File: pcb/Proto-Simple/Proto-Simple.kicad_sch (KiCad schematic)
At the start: 21 parts, among them J1 Conn_01x04, J10 Conn_01x01, J11 Conn_01x01, J12 Conn_01x01, J13 Conn_01x01, J2 Conn_01x01, J3 Conn_01x01, J4 Conn_01x01, J41 Conn_01x01, J42 Conn_01x01, J43 Conn_01x01, J44 Conn_01x01, J45 Conn_01x01, J46 Conn_01x01, J47 Conn_01x01, J5 Conn_01x01, J6 Conn_01x01, J7 Conn_01x01, J8 Conn_01x01, J9 Conn_01x01

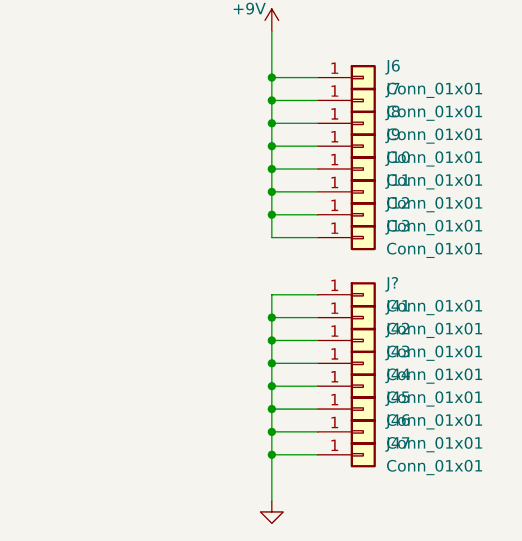
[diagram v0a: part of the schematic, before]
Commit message: [ProtoSimple] update Schematic
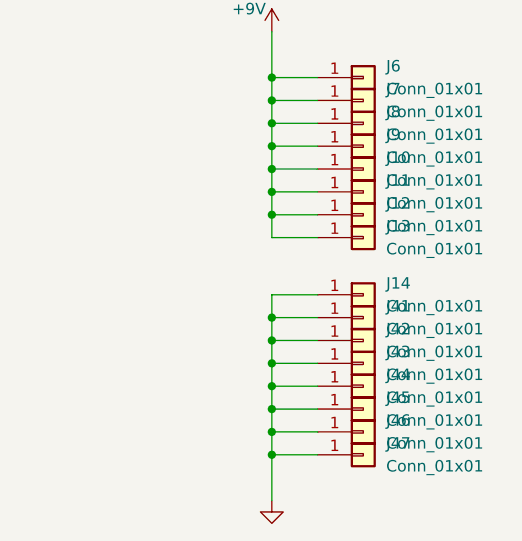
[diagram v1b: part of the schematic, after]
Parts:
- gave numbers to parts that had none: 1
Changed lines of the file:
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@@
   (symbol (lib_id "Connector_Generic:Conn_01x01") (at 163.83 119.38 0) (unit 1)
     (in_bom yes) (on_board yes) (fields_autoplaced)
-    (property "Reference" "J?" (id 0) (at 166.37 118.1099 0)
+    (property "Reference" "J14" (id 0) (at 166.37 118.1099 0)
       (effects (font (size 1.27 1.27)) (justify left))
     )
@@
       (reference "J13") (unit 1) (value "Conn_01x01") (footprint "MeineBib:Protopin")
     )
+    (path "/f7a1fee7-d81c-4e02-8116-b09f7e2d95c2"
+      (reference "J14") (unit 1) (value "Conn_01x01") (footprint "MeineBib:Protopin")
+    )
     (path "/2f3efa35-c3e1-45a2-83bc-04184a4ef9cc"
       (reference "J41") (unit 1) (value "Conn_01x01") (footprint "MeineBib:Protopin")
@@
       (reference "J47") (unit 1) (value "Conn_01x01") (footprint "MeineBib:Protopin")
     )
-    (path "/f7a1fee7-d81c-4e02-8116-b09f7e2d95c2"
-      (reference "J?") (unit 1) (value "Conn_01x01") (footprint "MeineBib:Protopin")
-    )
   )

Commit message: [All] Add LCSC part number for JST connector
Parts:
- J1: value Conn_01x04 -> (none); footprint Connector_JST:JST_XH_B4B-XH-A_1x04_P2.50mm_Vertical -> (none); LCSC^ (none) -> C144395; now in the parts list
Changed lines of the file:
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@@
   )
   (symbol (lib_id "Connector_Generic:Conn_01x04") (at 48.26 29.21 0) (mirror x) (unit 1)
-    (in_bom no) (on_board yes)
+    (in_bom yes) (on_board yes)
     (property "Reference" "J1" (id 0) (at 51.435 29.2101 0)
       (effects (font (size 1.27 1.27)) (justify left))
     )
-    (property "Value" "Conn_01x04" (id 1) (at 44.45 21.59 0)
+    (property "Value" "" (id 1) (at 44.45 21.59 0)
       (effects (font (size 1.27 1.27)) (justify left))
     )
-    (property "Footprint" "Connector_JST:JST_XH_B4B-XH-A_1x04_P2.50mm_Vertical" (id 2) (at 48.26 29.21 0)
+    (property "Footprint" "" (id 2) (at 48.26 29.21 0)
       (effects (font (size 1.27 1.27)) hide)
     )
@@
       (effects (font (size 1.27 1.27)) hide)
     )
+    (property "LCSC^" "C144395" (id 4) (at 48.26 29.21 0)
+      (effects (font (size 1.27 1.27)) hide)
+    )

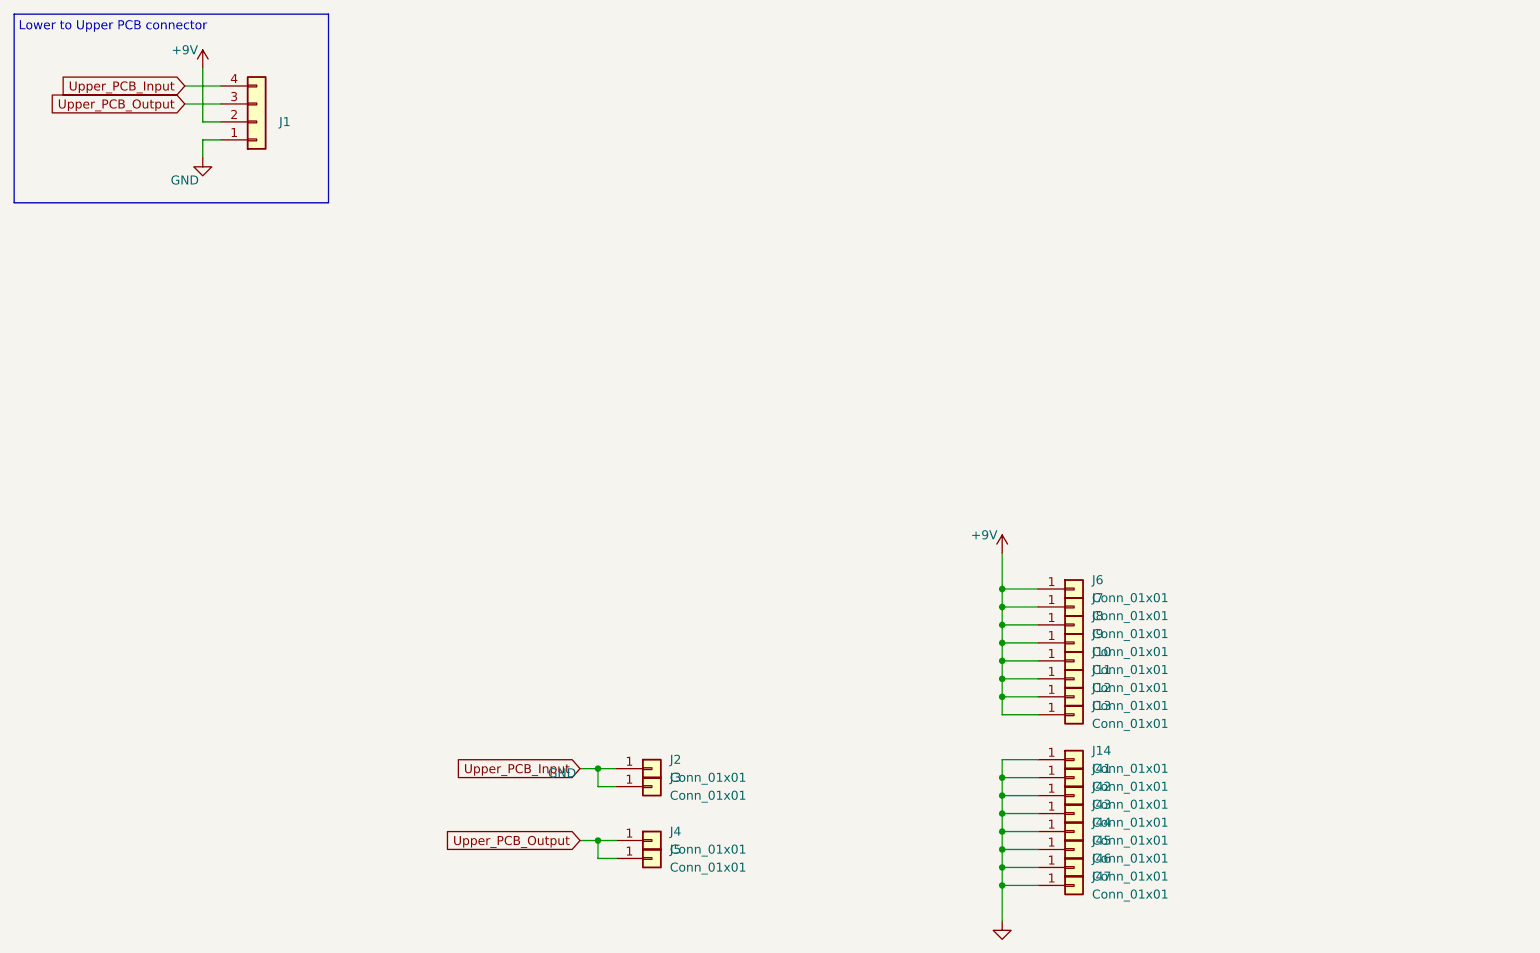
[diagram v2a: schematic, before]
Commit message: [ProtoSimple] Recreate PCB according to new base template
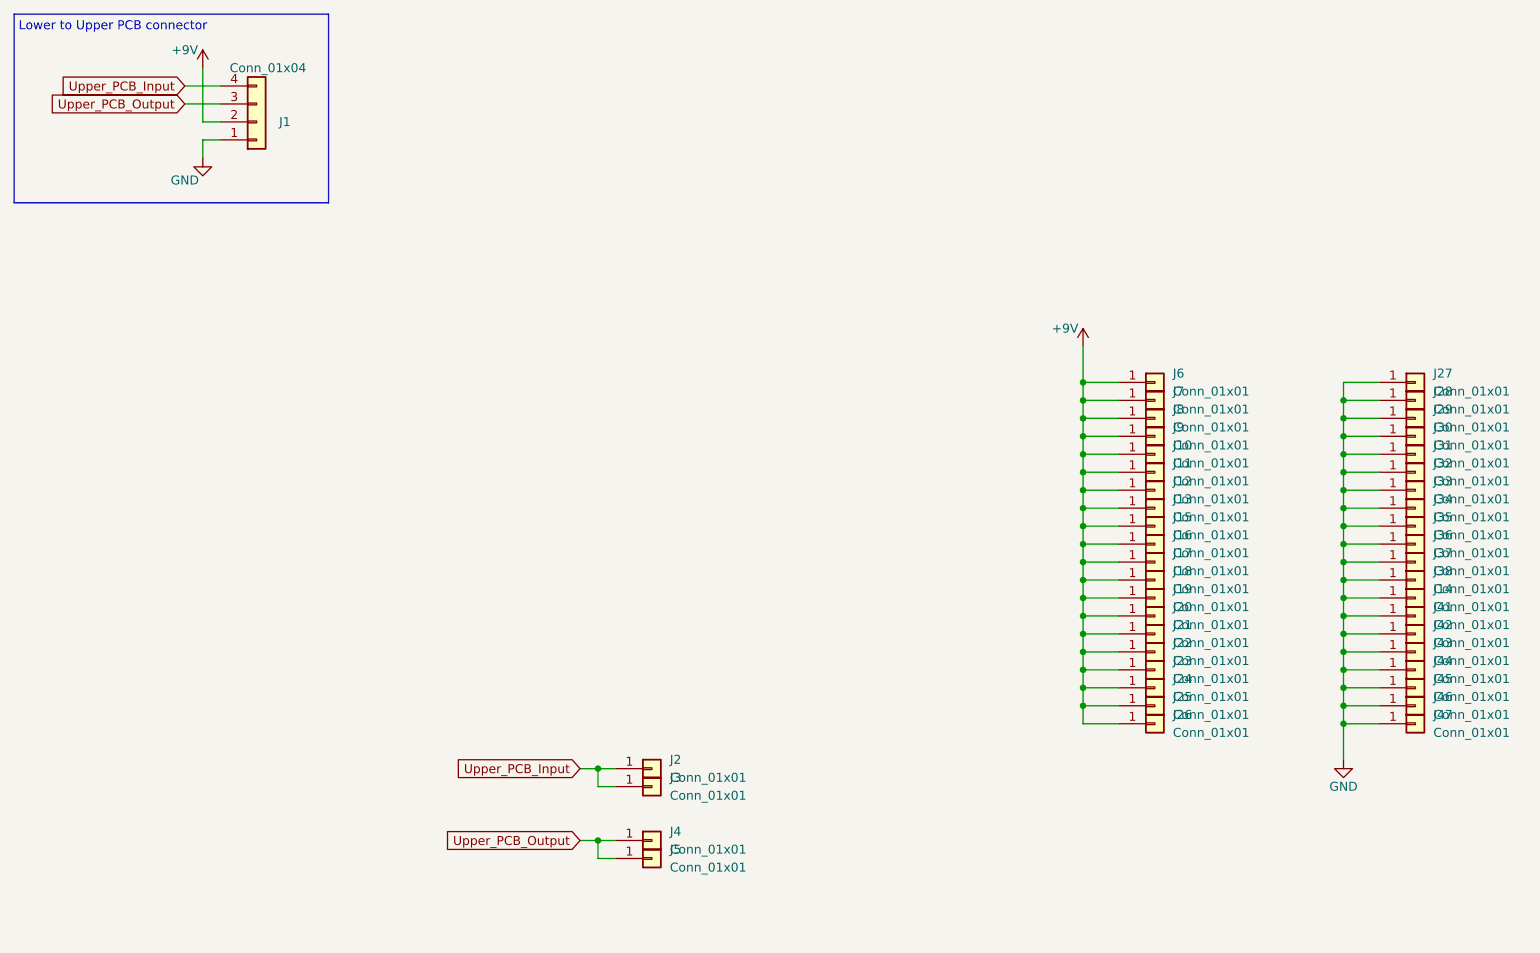
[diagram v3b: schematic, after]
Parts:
- added J15, J16, J17, J18, J19, J20, J21, J22, J23, J24, J25, J26, J27, J28, J29, J30, J31, J32, J33, J34, J35, J36, J37, J38: Conn_01x01, symbol Connector_Generic:Conn_01x01
- J1: value (none) -> Conn_01x04; footprint (none) -> Connector_JST:JST_XH_B4B-XH-A_1x04_P2.50mm_Vertical
- J10, J11, J12, J13, J14, J2, J3, J4, J41, J42, J43, J44, J45, J46, J47, J5, J6, J7, J8, J9: footprint MeineBib:Protopin -> (none)
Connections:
- net +9V: now also J15.1 (Pin_1), J16.1 (Pin_1), J17.1 (Pin_1), J18.1 (Pin_1), J19.1 (Pin_1), J20.1 (Pin_1), J21.1 (Pin_1), J22.1 (Pin_1), J23.1 (Pin_1), J24.1 (Pin_1), J25.1 (Pin_1), J26.1 (Pin_1)
- net GND: now also J27.1 (Pin_1), J28.1 (Pin_1), J29.1 (Pin_1), J30.1 (Pin_1), J31.1 (Pin_1), J32.1 (Pin_1), J33.1 (Pin_1), J34.1 (Pin_1), J35.1 (Pin_1), J36.1 (Pin_1), J37.1 (Pin_1), J38.1 (Pin_1)
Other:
- moved on the sheet: J10, J11, J12, J13, J14, J41, J42, J43, J44, J45, J46, J47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

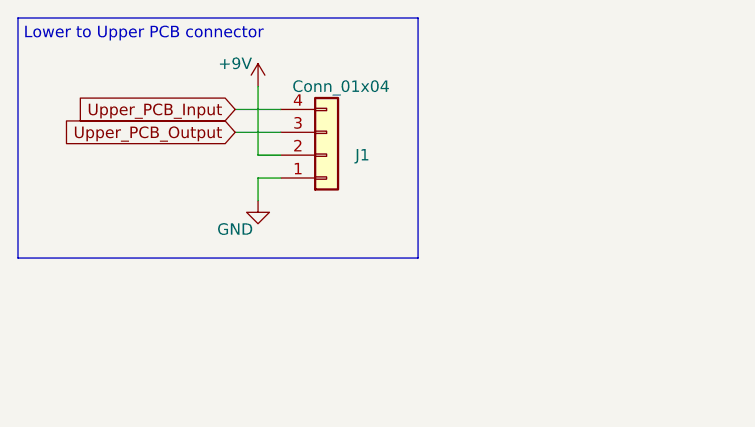
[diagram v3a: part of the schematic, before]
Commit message: [All] Flip board to board connector on upper PCB (obstructed some silk)
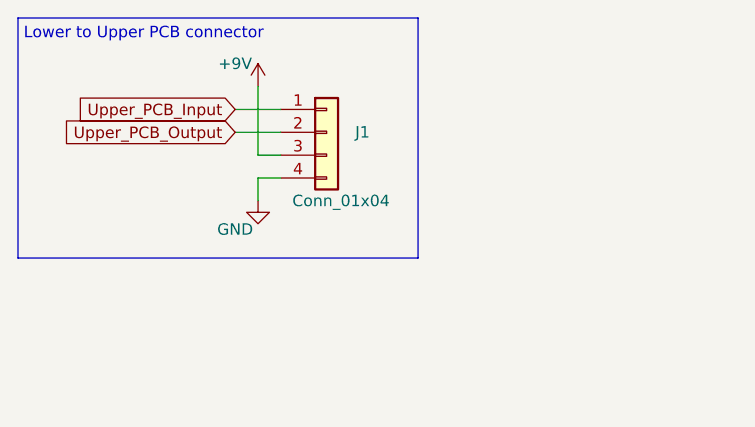
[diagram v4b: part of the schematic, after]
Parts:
- J10, J11, J12, J13, J14, J15, J16, J17, J18, J19, J2, J20, J21, J22, J23, J24, J25, J26, J27, J28, J29, J3, J30, J31, J32, J33, J34, J35, J36, J37, J38, J4, J41, J42, J43, J44, J45, J46, J47, J5, J6, J7, J8, J9: footprint (none) -> MeineBib:Protopin_Small
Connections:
- net +9V: now also J1.3 (Pin_3); no longer J1.2 (Pin_2)
- net GND: now also J1.4 (Pin_4); no longer J1.1 (Pin_1)
- net Upper_PCB_Input: now also J1.1 (Pin_1); no longer J1.4 (Pin_4)
- net Upper_PCB_Output: now also J1.2 (Pin_2); no longer J1.3 (Pin_3)
